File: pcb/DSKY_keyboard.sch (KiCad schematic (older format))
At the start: 60 parts, among them CN1 4U#20329, IC1 ATSAMD21E, J1 MOUNTINGHOLE3.0, J2 MOUNTINGHOLE3.0, J6 MOUNTINGHOLE3.0, J8 MOUNTINGHOLE3.0, Q1 reset, U1 AP2112K-3.3, U2 AQY232SZ

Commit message: Issue #1
Board now has (CLR) on PA00; backlighting always on. V3 board
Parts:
- removed R10: 1.1K, Trinket M0 rev D:0603-NO, symbol eagle:RESISTOR_0603_NOOUT
- removed U2: AQY232SZ, Package_SO:SO-4_4.4x4.3mm_P2.54mm, symbol DSKY_keyboard:AQY232SZ-Trinket_M0_rev_D-eagle-import
- D1, D2: value SCHOTTKY -> SCHOTTKY 30V
- JP2: value 20021221-00010C4LF -> 3221-10-0300-00-TR
- R1: value 10K -> 1.5K
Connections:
- net labels removed: +3.3V
- wire segments 208 -> 200
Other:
- note removed: "Very bright 0603~\nUse 10K"
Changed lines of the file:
@@
 Sheet 1 1
 Title "DSKY Keyboard Replica"
-Date "2020-07-09"
-Rev "2.0"
-Comp ""
+Date "2020-08-16"
+Rev "V3"
+Comp "DSKY-matic Project"
 Comment1 ""
 Comment2 ""
@@
 	16250 2500 16250 2250
 Wire Wire Line
-	18450 8800 18450 8750
-Wire Wire Line
 	12950 8750 12450 8750
 Wire Wire Line
@@
 P 6950 9650
 F 0 "R1" H 6950 9750 50  0000 C CNN
-F 1 "10K" H 6950 9650 40  0000 C CNB
+F 1 "1.5K" H 6950 9650 40  0000 C CNB
 F 2 "Trinket M0 rev D:0603-NO" H 6950 9650 50  0001 C CNN
 F 3 "" H 6950 9650 50  0001 C CNN
@@
 P 4450 9150
 F 0 "D2" H 4350 9250 42  0000 L BNN
-F 1 "SCHOTTKY" H 4350 9000 42  0000 L BNN
+F 1 "SCHOTTKY 30V " H 4350 9000 42  0000 L BNN
 F 2 "Trinket M0 rev D:SOD-123FL" H 4450 9150 50  0001 C CNN
 F 3 "" H 4450 9150 50  0001 C CNN
@@
 P 3950 9150
 F 0 "D1" H 3850 9250 42  0000 L BNN
-F 1 "SCHOTTKY" H 3850 9000 42  0000 L BNN
+F 1 "SCHOTTKY 30V " H 3850 9000 42  0000 L BNN
 F 2 "Trinket M0 rev D:SOD-123FL" H 3950 9150 50  0001 C CNN
 F 3 "" H 3950 9150 50  0001 C CNN
@@
 L power:GND #GND01
 U 1 1 5E3DB80E
-P 1550 2950
-F 0 "#GND01" H 1550 2950 50  0001 C CNN
-F 1 "GND" H 1450 2850 59  0000 L BNN
-F 2 "" H 1550 2950 50  0001 C CNN
-F 3 "" H 1550 2950 50  0001 C CNN
-	1    1550 2950
+P 1550 2850
+F 0 "#GND01" H 1550 2850 50  0001 C CNN
+F 1 "GND" H 1450 2750 59  0000 L BNN
+F 2 "" H 1550 2850 50  0001 C CNN
+F 3 "" H 1550 2850 50  0001 C CNN
+	1    1550 2850
 	1    0    0    -1
 $EndComp
@@
 L power:GND #GND04
 U 1 1 5E3DB826
-P 2150 5950
-F 0 "#GND04" H 2150 5950 50  0001 C CNN
-F 1 "GND" H 2050 5850 59  0000 L BNN
-F 2 "" H 2150 5950 50  0001 C CNN
-F 3 "" H 2150 5950 50  0001 C CNN
-	1    2150 5950
+P 2150 5850
+F 0 "#GND04" H 2150 5850 50  0001 C CNN
+F 1 "GND" H 2050 5750 59  0000 L BNN
+F 2 "" H 2150 5850 50  0001 C CNN
+F 3 "" H 2150 5850 50  0001 C CNN
+	1    2150 5850
 	-1   0    0    -1
 $EndComp
@@
 	1    0    0    -1
 $EndComp
-Text Notes 6250 9950 0    59   ~ 0
-Very bright 0603~\nUse 10K
 Text GLabel 7350 4250 2    50   Input ~ 0
 PA14
@@
 	19050 5950 18700 5950
 Wire Wire Line
-	14500 1500 15000 1500
-Wire Wire Line
 	15000 1500 15000 2250
 Wire Wire Line
@@
 Wire Wire Line
 	19000 8750 18450 8750
-Connection ~ 18450 8750
 Wire Wire Line
 	18450 8750 18450 8700
@@
 Wire Wire Line
 	4450 8550 4450 9050
-$Comp
-L DSKY_keyboard:AQY232SZ-Trinket_M0_rev_D-eagle-import U2
-U 1 1 5E5D7CBE
-P 10800 5700
-F 0 "U2" H 10800 6025 50  0000 C CNN
-F 1 "AQY232SZ" H 10800 5934 50  0000 C CNN
-F 2 "Package_SO:SO-4_4.4x4.3mm_P2.54mm" H 10600 5500 50  0001 L CIN
-F 3 "https://www.digikey.com/product-detail/en/panasonic-electric-works/AQY232SZ/255-2690-1-ND/2125790" H 10750 5700 50  0001 L CNN
-	1    10800 5700
-	1    0    0    -1
-$EndComp
-Wire Wire Line
-	10550 5600 10500 5600
-Wire Wire Line
-	10100 5600 9800 5600
-$Comp
-L power:GND #PWR0101
-U 1 1 5E5F1DF1
-P 10450 6150
-F 0 "#PWR0101" H 10450 5900 50  0001 C CNN
-F 1 "GND" H 10455 5977 50  0000 C CNN
-F 2 "" H 10450 6150 50  0001 C CNN
-F 3 "" H 10450 6150 50  0001 C CNN
-	1    10450 6150
-	1    0    0    -1
-$EndComp
-Wire Wire Line
-	10500 5800 10450 5800
-Wire Wire Line
-	11100 5800 11250 5800
-Wire Wire Line
-	11250 5800 11250 6100
-Wire Wire Line
-	11250 6100 10450 6100
-Wire Wire Line
-	10450 5800 10450 6100
-Connection ~ 10450 6100
-Wire Wire Line
-	10450 6100 10450 6150
+Wire Wire Line
+	15000 1500 14700 1500
 $Comp
 L eagle:RESISTOR_0603_NOOUT R6
@@
 $EndComp
 $Comp
-L eagle:RESISTOR_0603_NOOUT R10
-U 1 1 5F089C0F
-P 10300 5600
-F 0 "R10" H 10300 5700 50  0000 C CNN
-F 1 "1.1K" H 10300 5600 40  0000 C CNB
-F 2 "Trinket M0 rev D:0603-NO" H 10300 5600 50  0001 C CNN
-F 3 "" H 10300 5600 50  0001 C CNN
-	1    10300 5600
-	-1   0    0    1
-$EndComp
-Connection ~ 10500 5600
-$Comp
 L eagle:RESISTOR_0603_NOOUT R2
 U 1 1 5F135A29
@@
 Wire Wire Line
 	12100 5100 11650 5100
-Wire Wire Line
-	11650 5100 11650 5600
 Connection ~ 11650 5600
-Wire Wire Line
-	11650 5600 11100 5600
 Wire Wire Line
 	12000 3050 11650 3050
@@
 	17350 5600 19600 5600
 NoConn ~ 3500 7400
-NoConn ~ 7450 13500
 Text GLabel 7350 3850 2    50   Input ~ 0
 PA11
@@
 P 8200 7350
 F 0 "JP2" H 8250 7728 50  0000 C CNN
-F 1 "20021221-00010C4LF" H 8250 7729 50  0001 C CNN
+F 1 "3221-10-0300-00-TR" H 8250 7729 50  0001 C CNN
 F 2 "20021221-00010C4LF" H 8200 7350 50  0001 L BNN
-F 3 "" H 8200 7350 50  0001 C CNN
+F 3 "https://media.digikey.com/pdf/Data%20Sheets/CNC%20Tech%20PDFs/3221-XX-0300-00-TR_Dwg.pdf" H 8200 7350 50  0001 C CNN
 	1    8200 7350
 	1    0    0    -1
@@
 $EndComp
 $Comp
-L power:+3.3V #PWR0103
+L eagle:3.3V #PWR0103
 U 1 1 5F08E785
 P 7600 7050
 F 0 "#PWR0103" H 7600 6900 50  0001 C CNN
-F 1 "+3.3V" H 7615 7223 50  0000 C CNN
+F 1 "3.3V" H 7615 7223 50  0000 C CNN
 F 2 "" H 7600 7050 50  0001 C CNN
 F 3 "" H 7600 7050 50  0001 C CNN
@@
 Wire Wire Line
 	6500 7400 6050 7400
-Text GLabel 9800 5600 0    50   Input ~ 0
+Text GLabel 14700 1500 0    50   Input ~ 0
 PA00
 Wire Wire Line
@@
 	1    0    0    -1
 $EndComp
-Entry Wire Line
-	15600 -650 15700 -550
-Entry Wire Line
-	15600 -650 15700 -550
-Entry Wire Line
-	15600 -650 15700 -550
-Entry Wire Line
-	15600 -650 15700 -550
-Entry Wire Line
-	15600 -650 15700 -550
-Entry Wire Line
-	15600 -650 15700 -550
-Entry Wire Line
-	15600 -650 15700 -550
-Entry Wire Line
-	15600 -650 15700 -550
-Entry Wire Line
-	15600 -650 15700 -550
-Entry Wire Line
-	15600 -650 15700 -550
-Entry Wire Line
-	15600 -650 15700 -550
-Entry Wire Line
-	15600 -650 15700 -550
-Entry Wire Line
-	15600 -650 15700 -550
-Entry Wire Line
-	15600 -700 15700 -600
-Entry Wire Line
-	15600 -700 15700 -600
-Entry Wire Line
-	15600 -700 15700 -600
-Entry Wire Line
-	15600 -700 15700 -600
-Entry Wire Line
-	15600 -700 15700 -600
-Entry Wire Line
-	15600 -700 15700 -600
-Entry Wire Line
-	15600 -700 15700 -600
-Entry Wire Line
-	15600 -700 15700 -600
-Entry Wire Line
-	15600 -700 15700 -600
-Entry Wire Line
-	15600 -700 15700 -600
-Entry Wire Line
-	15600 -700 15700 -600
-Entry Wire Line
-	15600 -700 15700 -600
-Entry Wire Line
-	15600 -700 15700 -600
-Entry Wire Line
-	15600 -700 15700 -600
-Entry Wire Line
-	15600 -700 15700 -600
-Entry Wire Line
-	15600 -700 15700 -600
-Entry Wire Line
-	15600 -700 15700 -600
-Entry Wire Line
-	15600 -700 15700 -600
-Entry Wire Line
-	15600 -700 15700 -600
-Entry Wire Line
-	15600 -700 15700 -600
-Entry Wire Line
-	15600 -700 15700 -600
-Entry Wire Line
-	15600 -700 15700 -600
-Entry Wire Line
-	15600 -700 15700 -600
-Entry Wire Line
-	15600 -700 15700 -600
-Entry Wire Line
-	15600 -700 15700 -600
-Entry Wire Line
-	15600 -700 15700 -600
-Entry Wire Line
-	15600 -700 15700 -600
-Entry Wire Line
-	15600 -700 15700 -600
-Entry Wire Line
-	15600 -700 15700 -600
-Entry Wire Line
-	15600 -700 15700 -600
-Entry Wire Line
-	15600 -700 15700 -600
-Entry Wire Line
-	15600 -700 15700 -600
-Entry Wire Line
-	15600 -700 15700 -600
-Entry Wire Line
-	15600 -700 15700 -600
-Entry Wire Line
-	15600 -700 15700 -600
-Text GLabel 14500 1500 0    50   Input ~ 0
-PA18
+NoConn ~ 5750 9850
+$Comp
+L power:GND #PWR0104
+U 1 1 5F405CF5
+P 12100 10900
+F 0 "#PWR0104" H 12100 10650 50  0001 C CNN
+F 1 "GND" H 12105 10727 50  0000 C CNN
+F 2 "" H 12100 10900 50  0001 C CNN
+F 3 "" H 12100 10900 50  0001 C CNN
+	1    12100 10900
+	1    0    0    -1
+$EndComp
+$Comp
+L power:GND #PWR0101
+U 1 1 5E5F1DF1
+P 10850 5800
+F 0 "#PWR0101" H 10850 5550 50  0001 C CNN
+F 1 "GND" H 10855 5627 50  0000 C CNN
+F 2 "" H 10850 5800 50  0001 C CNN
+F 3 "" H 10850 5800 50  0001 C CNN
+	1    10850 5800
+	1    0    0    -1
+$EndComp
+Wire Wire Line
+	11650 5100 11650 5600
+Wire Wire Line
+	11650 5600 10850 5600
+Wire Wire Line
+	10850 5600 10850 5800
 $EndSCHEMATC

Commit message: Update J-Link Header PCB Footprint
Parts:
- JP2: footprint 20021221-00010C4LF -> Trinket M0 rev D:3221-10-0300-00-TR
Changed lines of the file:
@@
 F 0 "JP2" H 8250 7728 50  0000 C CNN
 F 1 "3221-10-0300-00-TR" H 8250 7729 50  0001 C CNN
-F 2 "20021221-00010C4LF" H 8200 7350 50  0001 L BNN
+F 2 "Trinket M0 rev D:3221-10-0300-00-TR" H 8200 7350 50  0001 L BNN
 F 3 "https://media.digikey.com/pdf/Data%20Sheets/CNC%20Tech%20PDFs/3221-XX-0300-00-TR_Dwg.pdf" H 8200 7350 50  0001 C CNN
 	1    8200 7350

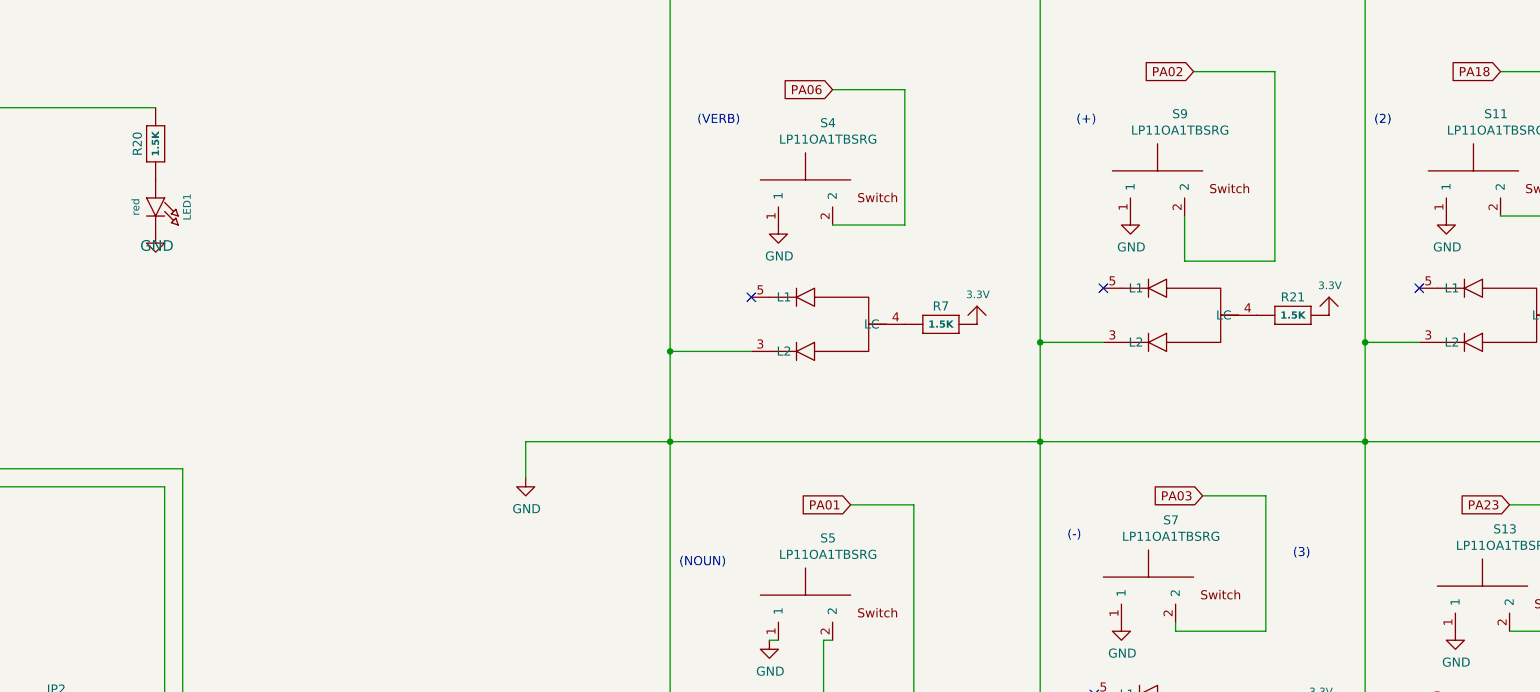
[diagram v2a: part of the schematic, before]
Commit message: V2 Board complete
V3 updates subsequent to full-up V2 board tests (incl. firmware)
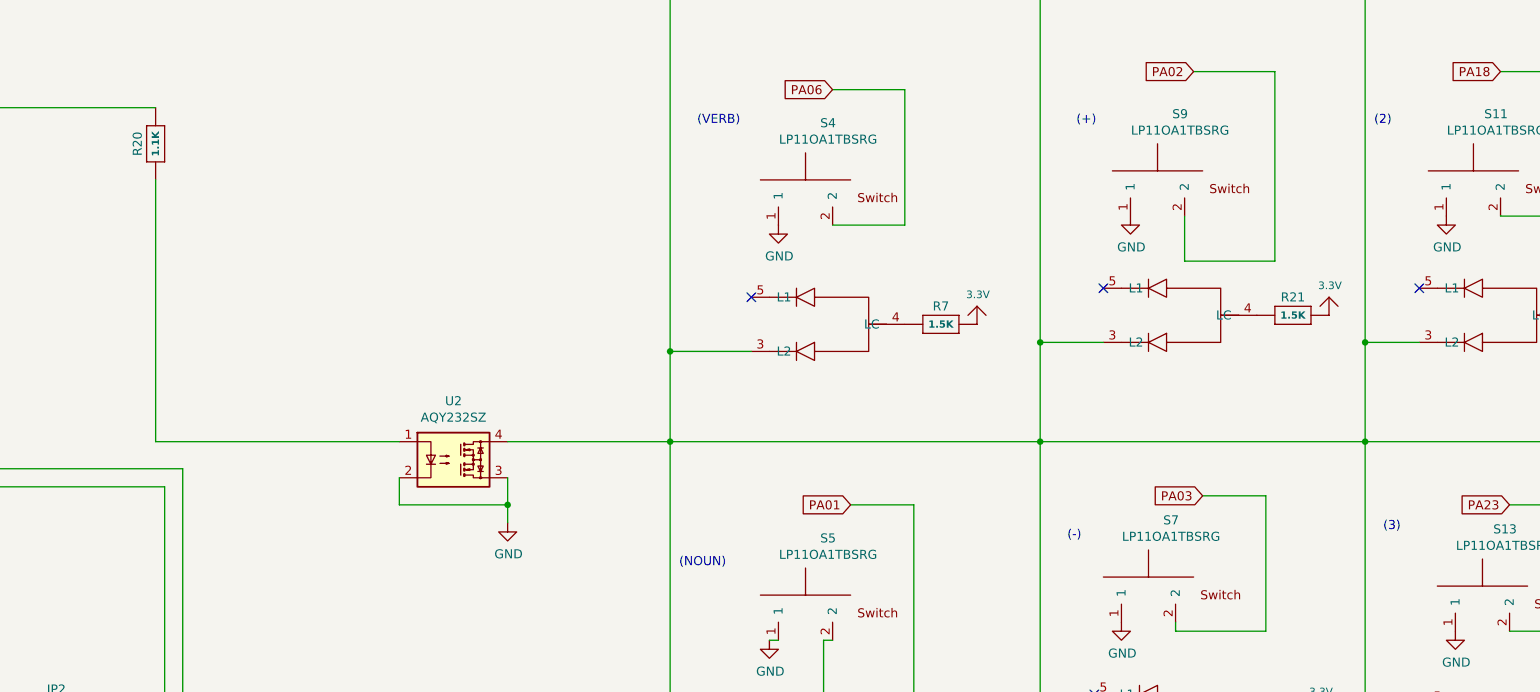
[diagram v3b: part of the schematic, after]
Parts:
- removed LED1: red, Trinket M0 rev D:CHIPLED_0603_NOOUTLINE, symbol eagle:LED0603_NOOUTLINE
- added U2: AQY232SZ, Package_SO:SO-4_4.4x4.3mm_P2.54mm, symbol DSKY_keyboard:AQY232SZ-Trinket_M0_rev_D-eagle-import
- R20: value 1.5K -> 1.1K
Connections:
- net GND: now also U2.2, U2.3; no longer S1.3 (L2), S10.3 (L2), S11.3 (L2), S12.3 (L2), S13.3 (L2), S14.3 (L2), S15.3 (L2), S16.3 (L2), S17.3 (L2), S18.3 (L2), S19.3 (L2), S2.3 (L2), S3.3 (L2), S4.3 (L2), S5.3 (L2), S6.3 (L2), S7.3 (L2), S8.3 (L2), S9.3 (L2)
- net at R20.1: now also U2.1
- new net: S1.3 (L2), S10.3 (L2), S11.3 (L2), S12.3 (L2), S13.3 (L2), S14.3 (L2), S15.3 (L2), S16.3 (L2), S17.3 (L2), S18.3 (L2), S19.3 (L2), S2.3 (L2), S3.3 (L2), S4.3 (L2), S5.3 (L2), S6.3 (L2), S7.3 (L2), S8.3 (L2), S9.3 (L2), U2.4
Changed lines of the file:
@@
 	1    0    0    -1
 $EndComp
-Text Notes 15100 6250 0    50   ~ 0
+Text Notes 15600 6100 0    50   ~ 0
 (3)
 Wire Wire Line
@@
 P 8800 3950
 F 0 "R20" H 8800 4050 50  0000 C CNN
-F 1 "1.5K" H 8800 3950 40  0000 C CNB
+F 1 "1.1K" H 8800 3950 40  0000 C CNB
 F 2 "Trinket M0 rev D:0603-NO" H 8800 3950 50  0001 C CNN
 F 3 "" H 8800 3950 50  0001 C CNN
 	1    8800 3950
 	0    -1   -1   0
-$EndComp
-$Comp
-L eagle:LED0603_NOOUTLINE LED1
-U 1 1 5F104D21
-P 8800 4350
-F 0 "LED1" H 8750 4525 42  0000 C CNN
-F 1 "red" H 8750 4240 42  0000 C CNN
-F 2 "Trinket M0 rev D:CHIPLED_0603_NOOUTLINE" H 8800 4350 50  0001 C CNN
-F 3 "" H 8800 4350 50  0001 C CNN
-	1    8800 4350
-	0    1    1    0
-$EndComp
-$Comp
-L power:GND #GND0101
-U 1 1 5F104D2B
-P 8800 4450
-F 0 "#GND0101" H 8800 4450 50  0001 C CNN
-F 1 "GND" H 8700 4350 59  0000 L BNN
-F 2 "" H 8800 4450 50  0001 C CNN
-F 3 "" H 8800 4450 50  0001 C CNN
-	1    8800 4450
-	-1   0    0    -1
 $EndComp
 Wire Wire Line
@@
 L power:GND #PWR0101
 U 1 1 5E5F1DF1
-P 10850 5800
-F 0 "#PWR0101" H 10850 5550 50  0001 C CNN
-F 1 "GND" H 10855 5627 50  0000 C CNN
-F 2 "" H 10850 5800 50  0001 C CNN
-F 3 "" H 10850 5800 50  0001 C CNN
-	1    10850 5800
+P 10750 6050
+F 0 "#PWR0101" H 10750 5800 50  0001 C CNN
+F 1 "GND" H 10755 5877 50  0000 C CNN
+F 2 "" H 10750 6050 50  0001 C CNN
+F 3 "" H 10750 6050 50  0001 C CNN
+	1    10750 6050
 	1    0    0    -1
 $EndComp
 Wire Wire Line
 	11650 5100 11650 5600
-Wire Wire Line
-	11650 5600 10850 5600
-Wire Wire Line
-	10850 5600 10850 5800
+$Comp
+L DSKY_keyboard:AQY232SZ-Trinket_M0_rev_D-eagle-import U2
+U 1 1 5F4E4F59
+P 10450 5700
+F 0 "U2" H 10450 6025 50  0000 C CNN
+F 1 "AQY232SZ" H 10450 5934 50  0000 C CNN
+F 2 "Package_SO:SO-4_4.4x4.3mm_P2.54mm" H 10250 5500 50  0001 L CIN
+F 3 "" H 10400 5700 50  0001 L CNN
+	1    10450 5700
+	1    0    0    -1
+$EndComp
+Wire Wire Line
+	11650 5600 10750 5600
+Wire Wire Line
+	10750 5800 10750 5950
+Wire Wire Line
+	10150 5800 10150 5950
+Wire Wire Line
+	10150 5950 10750 5950
+Connection ~ 10750 5950
+Wire Wire Line
+	10750 5950 10750 6050
+Wire Wire Line
+	8800 4150 8800 5600
+Wire Wire Line
+	8800 5600 10150 5600
 $EndSCHEMATC
